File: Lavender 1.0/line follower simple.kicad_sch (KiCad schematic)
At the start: 40 parts, among them J1 XT30UPB-M, J2 Conn_01x06_Socket, J5 Conn_01x06_Socket, J6 Conn_02x06_Counter_Clockwise, J7 Conn_02x06_Counter_Clockwise, SW2 SW_Push, SW5 SW_Push_DPDT, SW6 SW_Push_DPDT, U21 BNO055

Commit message: started routing
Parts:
- removed D1, D2: LED, LED_THT:LED_D5.0mm, symbol Device:LED
- removed J2, J5: Conn_01x06_Socket, Connector_JST:JST_SH_BM06B-SRSS-TB_1x06-1MP_P1.00mm_Vertical, symbol Connector:Conn_01x06_Socket
- removed J6, J7: Conn_02x06_Counter_Clockwise, Connector_IDC:IDC-Header_2x06_P2.54mm_Vertical_SMD, symbol Connector_Generic:Conn_02x06_Counter_Clockwise
- removed JP1, JP10, JP11, JP12, JP13, JP14, JP15, JP16, JP17, JP18, JP19, JP2, JP20, JP3, JP4, JP5, JP6, JP7, JP8, JP9: SolderJumper_2_Open, Jumper:SolderJumper-2_P1.3mm_Open_RoundedPad1.0x1.5mm, symbol Jumper:SolderJumper_2_Open
- removed R1, R2: 47, Resistor_SMD:R_0603_1608Metric_Pad0.98x0.95mm_HandSolder, symbol Device:R
- removed U21: BNO055, customs:BNO055 module, symbol RM_Footprints:BNO055_7Semi_Module
- added H1, H2, H3, H4: MountingHole, customs:2mm hole, symbol Mechanical:MountingHole
- added J14, J15, J2: Conn_01x20, Connector_FFC-FPC:Amphenol_F32Q-1A7x1-11020_1x20-1MP_P0.5mm_Horizontal, symbol Connector_Generic:Conn_01x20
- added J3, J4: Conn_01x02_Pin, Connector_PinHeader_2.54mm:PinHeader_1x02_P2.54mm_Vertical, symbol Connector:Conn_01x02_Pin
- added U1: 74HC4067, customs:74HC4067-Mux, symbol customs:74HC4067
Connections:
- net +3.3V: now also J14.1 (Pin_1), J14.19 (Pin_19), J14.20 (Pin_20), J15.1 (Pin_1), J15.2 (Pin_2), J15.20 (Pin_20), J2.1 (Pin_1), J2.19 (Pin_19), J2.20 (Pin_20), U1.P24 (VCC)
- net AIN1: no longer TB1.6 (AIN1)
- net AIN2: no longer TB1.7 (AIN2)
- net BAT+: no longer SW5.2 (B), SW5.5 (B)
- net BIN1: no longer TB1.4 (BIN1)
- net BIN2: no longer TB1.3 (BIN2)
- net GND: now also J14.11 (Pin_11), J14.13 (Pin_13), J14.15 (Pin_15), J14.17 (Pin_17), J14.18 (Pin_18), J14.2 (Pin_2), J14.3 (Pin_3), J14.5 (Pin_5), J14.6 (Pin_6), J14.7 (Pin_7), J14.8 (Pin_8), J14.9 (Pin_9), J15.10 (Pin_10), J15.12 (Pin_12), J15.14 (Pin_14), J15.16 (Pin_16), J15.18 (Pin_18), J15.4 (Pin_4), J15.6 (Pin_6), J15.8 (Pin_8), J2.11 (Pin_11), J2.13 (Pin_13), J2.15 (Pin_15), J2.17 (Pin_17), J2.3 (Pin_3), J2.5 (Pin_5), J2.7 (Pin_7), J2.9 (Pin_9), U1.P12 (GND), U1.P15 (EN)
- net Motor1+: now also J3.1 (Pin_1); no longer TB1.13 (M1Out+)
- net Motor1-: now also J3.2 (Pin_2); no longer TB1.12 (M1Out-)
- net Motor2+: now also J4.1 (Pin_1); no longer TB1.10 (M2Out+)
- net Motor2-: now also J4.2 (Pin_2); no longer TB1.11 (M2Out-)
- net PWMA: no longer TB1.8 (PWMA)
- net PWMB: no longer TB1.2 (PWMB)
- net Q1: now also U1.P9 (CHAN0)
- net Q2: now also U1.P8 (CHAN1)
- net Q3: now also U1.P7 (CHAN2)
- net Q4: now also U1.P6 (CHAN3)
- net Q5: now also U1.P5 (CHAN4)
- net Q6: now also U1.P4 (CHAN5)
- net Q7: now also U1.P3 (CHAN6)
- net Q8: now also U1.P2 (CHAN7)
- net Q9: now also U1.P23 (CHAN8)
- net SNSR1: now also J15.3 (Pin_3)
- net SNSR2: now also J15.5 (Pin_5)
- net SNSR3: now also J15.7 (Pin_7)
- net SNSR4: now also J15.9 (Pin_9)
- net SNSR5: now also J15.13 (Pin_13)
- net SNSR6: now also J15.15 (Pin_15)
- net SNSR7: now also J15.17 (Pin_17)
- net SNSR8: now also J15.19 (Pin_19)
- net SNSR9: now also J15.11 (Pin_11)
- net T1: now also J2.18 (Pin_18)
- net T2: now also J2.16 (Pin_16)
- net T3: now also J2.14 (Pin_14)
- net T4: now also J2.12 (Pin_12)
- net T5: now also J2.8 (Pin_8)
- net T6: now also J2.6 (Pin_6)
- net T7: now also J2.4 (Pin_4)
- net T8: now also J2.2 (Pin_2)
- net T9: now also J2.10 (Pin_10)
- net IMU_RST: no longer names the net of BlackPill1.4 (PB10)
- net IMU_SCL: no longer names the net of BlackPill1.36 (PB8)
- net IMU_SDA: no longer names the net of BlackPill1.37 (PB9)
- net LED: no longer names the net of BlackPill1.30 (PA15)
- new net AIN1_t: TB1.6 (AIN1)
- new net AIN2_t: TB1.7 (AIN2)
- new net BAT+_t: SW5.2 (B), SW5.5 (B)
- new net BIN1_t: TB1.4 (BIN1)
- new net BIN2_t: TB1.3 (BIN2)
- new net COM_mux: J14.4 (Pin_4), U1.P1 (COM)
- new net Motor1+_t: TB1.13 (M1Out+)
- new net Motor1-_t: TB1.12 (M1Out-)
- new net Motor2+_t: TB1.10 (M2Out+)
- new net Motor2-_t: TB1.11 (M2Out-)
- new net PWMA_t: TB1.8 (PWMA)
- new net PWMB_t: TB1.2 (PWMB)
- new net Q10: U1.P22 (CHAN9)
- new net Q11: U1.P21 (CHAN10)
- new net Q12: U1.P20 (CHAN11)
- new net Q13: U1.P19 (CHAN12)
- new net Q14: U1.P18 (CHAN13)
- new net Q15: U1.P17 (CHAN14)
- new net Q16: U1.P16 (CHAN15)
- new net S0_mux: J14.16 (Pin_16), U1.P10 (S0)
- new net S1_mux: J14.14 (Pin_14), U1.P11 (S1)
- new net S2_mux: J14.12 (Pin_12), U1.P14 (S2)
- new net S3_mux: J14.10 (Pin_10), U1.P13 (S3)
- no-connect marks 21 -> 20
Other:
- added sheet Layer connectors (layerconnect.kicad_sch)
- note added: "Mounting holes"
- note added: "Multiplexer"
- note removed: "BNO055 Module"
- note removed: "LEDs"
- note removed: "Sensor Power bus"
- moved on the sheet: BT2, SW5, SW6

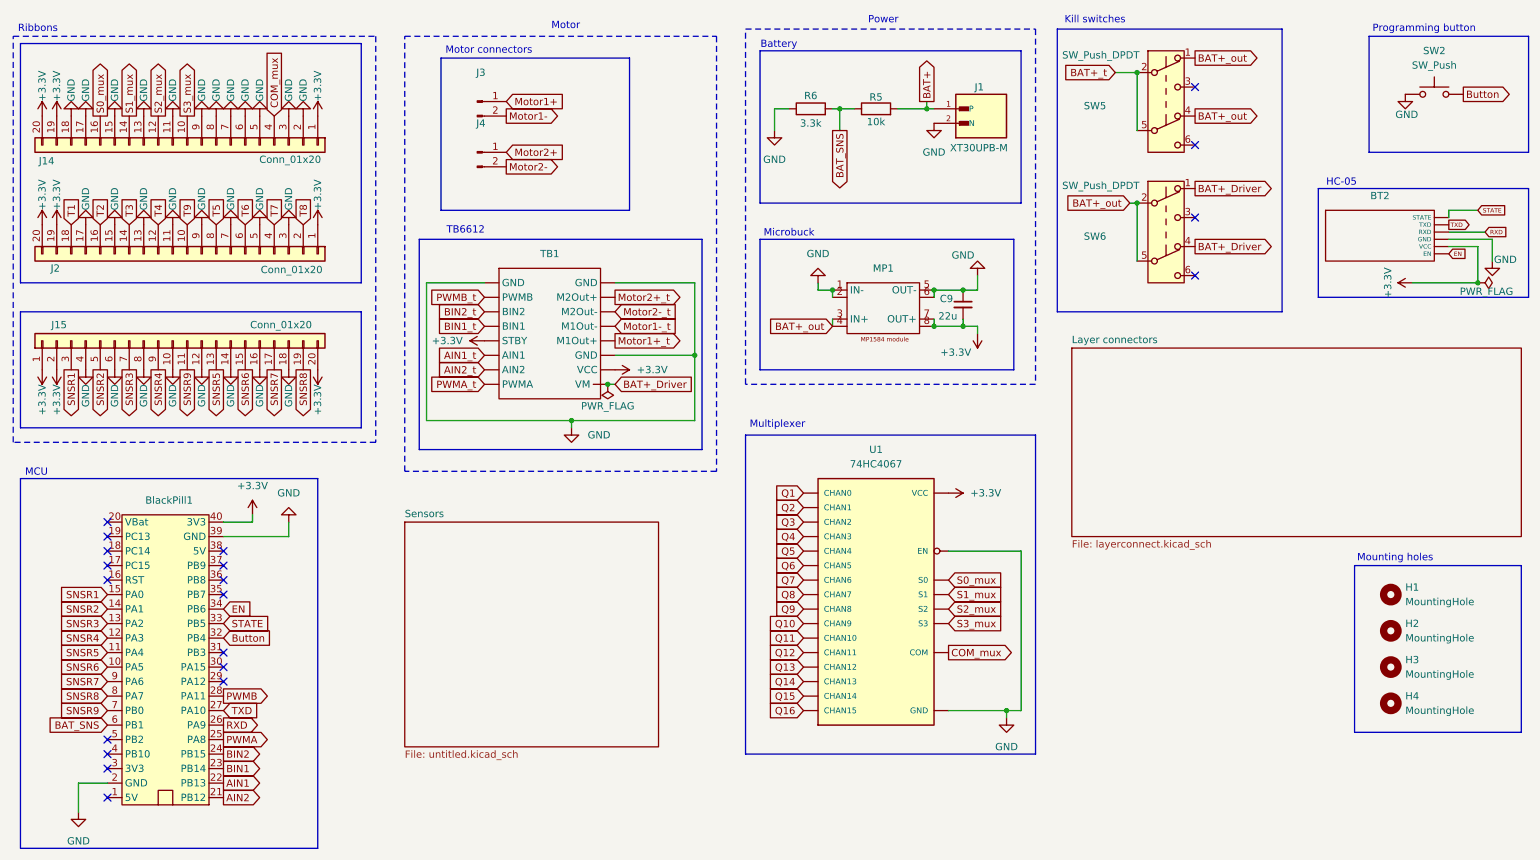
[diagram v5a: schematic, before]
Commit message: Finished 16 sensor array
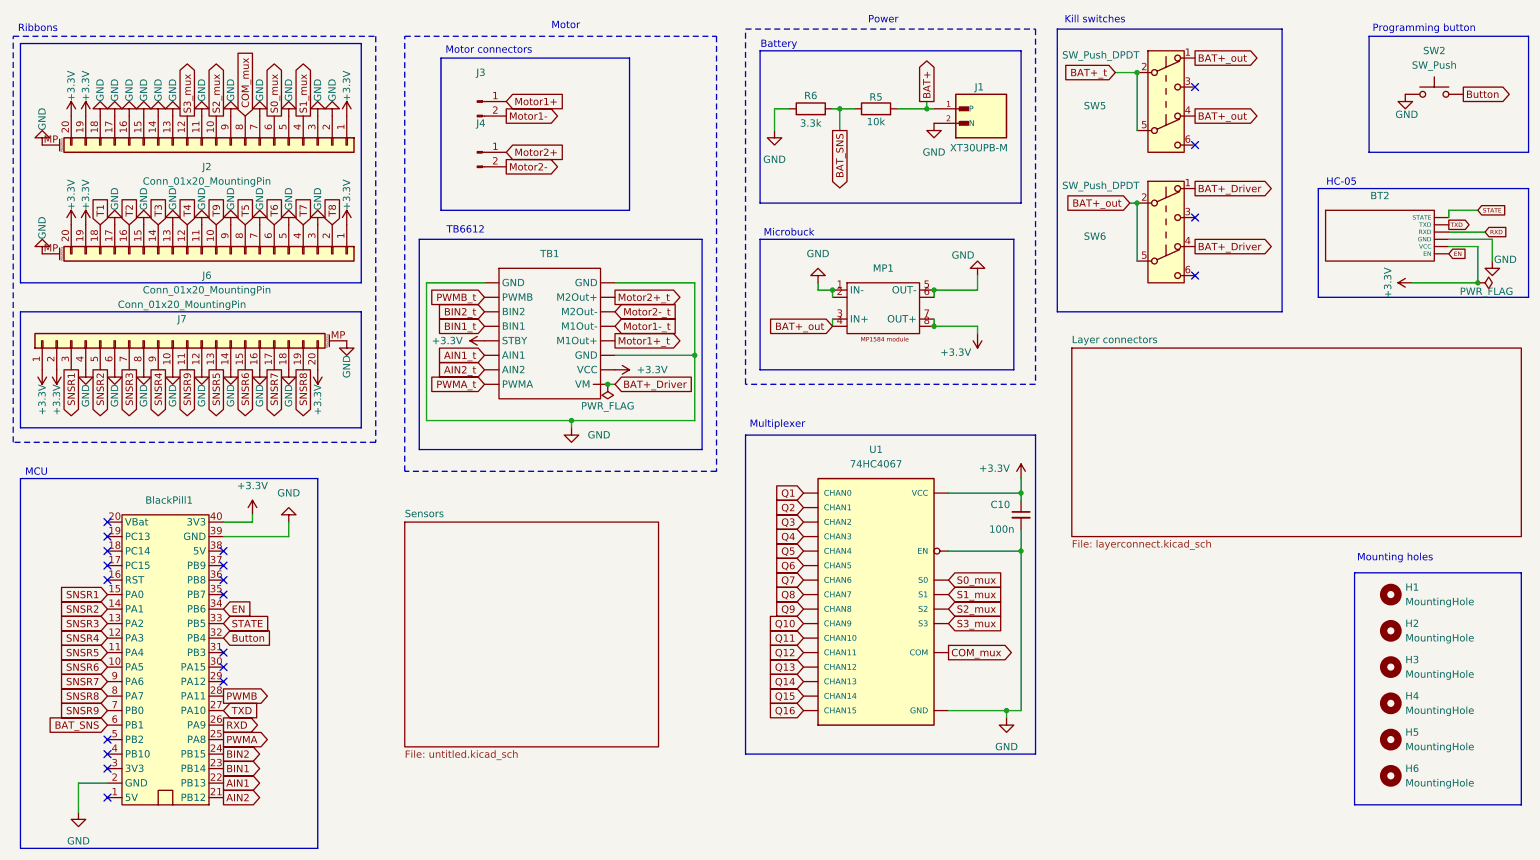
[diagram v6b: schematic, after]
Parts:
- removed C9: 22u, Capacitor_SMD:C_0603_1608Metric_Pad1.08x0.95mm_HandSolder, symbol Device:C_Small
- removed J14, J15, J2: Conn_01x20, Connector_FFC-FPC:Amphenol_F32Q-1A7x1-11020_1x20-1MP_P0.5mm_Horizontal, symbol Connector_Generic:Conn_01x20
- added C10: 100n, Capacitor_SMD:C_0603_1608Metric_Pad1.08x0.95mm_HandSolder, symbol Device:C_Small
- added H5, H6: MountingHole, customs:2mm hole, symbol Mechanical:MountingHole
- added J2, J6, J7: Conn_01x20_MountingPin, Connector_FFC-FPC:Amphenol_F32Q-1A7x1-11020_1x20-1MP_P0.5mm_Horizontal, symbol Connector_Generic_MountingPin:Conn_01x20_MountingPin
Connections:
- net +3.3V: now also C10.1, J2.1 (Pin_1), J2.19 (Pin_19), J2.20 (Pin_20), J6.1 (Pin_1), J6.19 (Pin_19), J6.20 (Pin_20), J7.1 (Pin_1), J7.2 (Pin_2), J7.20 (Pin_20)
- net COM_mux: now also J2.8 (Pin_8)
- net GND: now also C10.2, J2.11 (Pin_11), J2.13 (Pin_13), J2.14 (Pin_14), J2.15 (Pin_15), J2.16 (Pin_16), J2.17 (Pin_17), J2.18 (Pin_18), J2.2 (Pin_2), J2.3 (Pin_3), J2.5 (Pin_5), J2.7 (Pin_7), J2.9 (Pin_9), J2.MP (MountPin), J6.11 (Pin_11), J6.13 (Pin_13), J6.15 (Pin_15), J6.17 (Pin_17), J6.3 (Pin_3), J6.5 (Pin_5), J6.7 (Pin_7), J6.9 (Pin_9), J6.MP (MountPin), J7.10 (Pin_10), J7.12 (Pin_12), J7.14 (Pin_14), J7.16 (Pin_16), J7.18 (Pin_18), J7.4 (Pin_4), J7.6 (Pin_6), J7.8 (Pin_8), J7.MP (MountPin)
- net S0_mux: now also J2.6 (Pin_6)
- net S1_mux: now also J2.4 (Pin_4)
- net S2_mux: now also J2.10 (Pin_10)
- net S3_mux: now also J2.12 (Pin_12)
- net SNSR1: now also J7.3 (Pin_3)
- net SNSR2: now also J7.5 (Pin_5)
- net SNSR3: now also J7.7 (Pin_7)
- net SNSR4: now also J7.9 (Pin_9)
- net SNSR5: now also J7.13 (Pin_13)
- net SNSR6: now also J7.15 (Pin_15)
- net SNSR7: now also J7.17 (Pin_17)
- net SNSR8: now also J7.19 (Pin_19)
- net SNSR9: now also J7.11 (Pin_11)
- net T1: now also J6.18 (Pin_18)
- net T2: now also J6.16 (Pin_16)
- net T3: now also J6.14 (Pin_14)
- net T4: now also J6.12 (Pin_12)
- net T5: now also J6.8 (Pin_8)
- net T6: now also J6.6 (Pin_6)
- net T7: now also J6.4 (Pin_4)
- net T8: now also J6.2 (Pin_2)
- net T9: now also J6.10 (Pin_10)

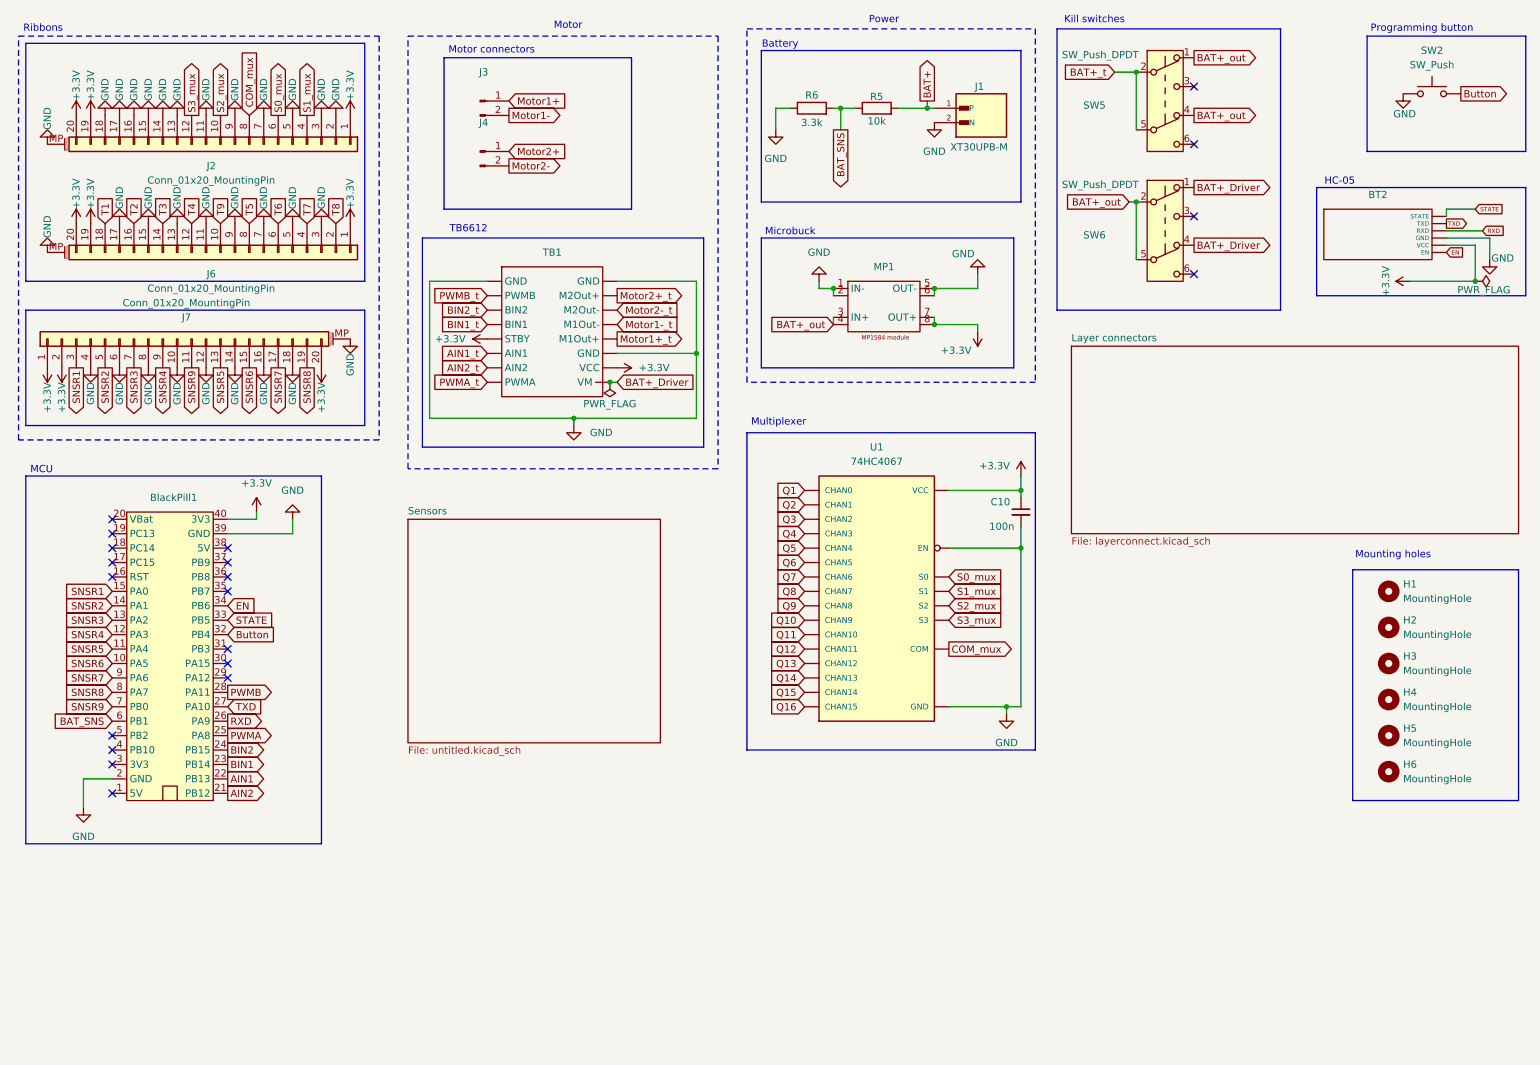
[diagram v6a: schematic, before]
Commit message: Start third sensor array
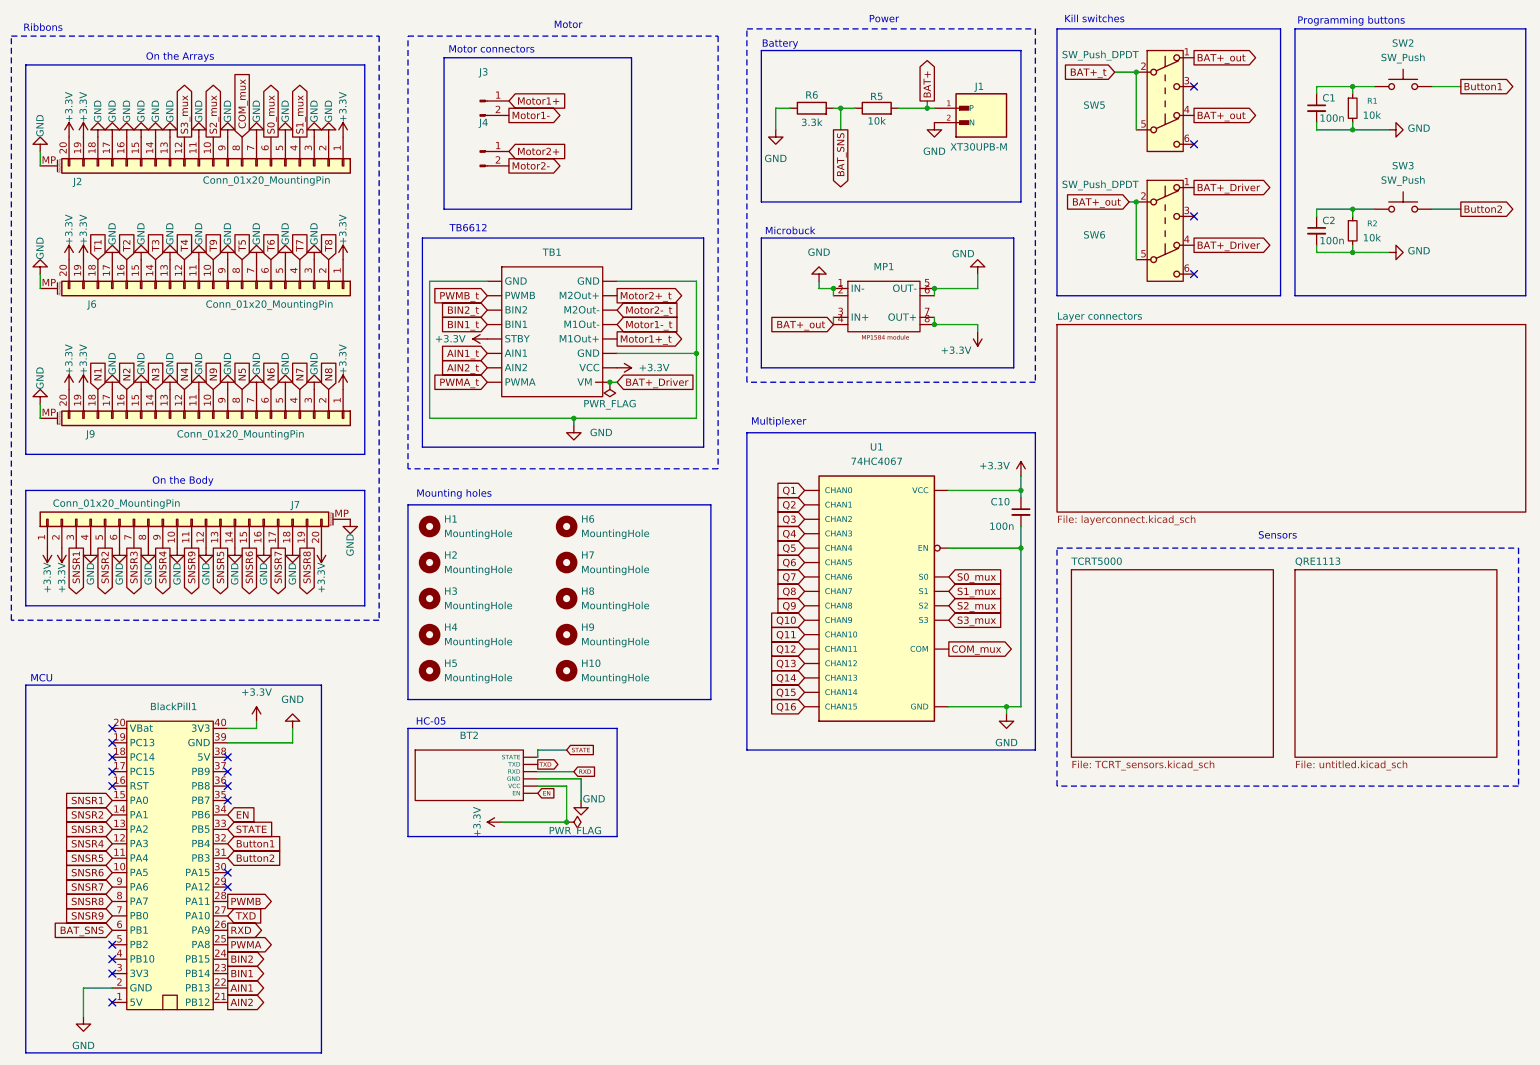
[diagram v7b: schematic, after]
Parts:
- added C1, C2: 100n, Capacitor_SMD:C_0603_1608Metric_Pad1.08x0.95mm_HandSolder, symbol Device:C_Small
- added H10, H7, H8, H9: MountingHole, customs:2mm hole, symbol Mechanical:MountingHole
- added J9: Conn_01x20_MountingPin, Connector_FFC-FPC:Amphenol_F32Q-1A7x1-11020_1x20-1MP_P0.5mm_Horizontal, symbol Connector_Generic_MountingPin:Conn_01x20_MountingPin
- added R1, R2: 10k, Resistor_SMD:R_0603_1608Metric_Pad0.98x0.95mm_HandSolder, symbol Device:R_Small
- added SW3: SW_Push, customs:Push button-fp, symbol Switch:SW_Push
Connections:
- net +3.3V: now also J9.1 (Pin_1), J9.19 (Pin_19), J9.20 (Pin_20)
- net GND: now also C1.2, C2.2, J9.11 (Pin_11), J9.13 (Pin_13), J9.15 (Pin_15), J9.17 (Pin_17), J9.3 (Pin_3), J9.5 (Pin_5), J9.7 (Pin_7), J9.9 (Pin_9), J9.MP (MountPin), R1.2, R2.2; no longer SW2.1
- net Button2: now reaches BlackPill1.31 (PB3)
- net Button2: now also SW3.2
- net Button renamed Button1
- new net: C1.1, R1.1, SW2.1
- new net: C2.1, R2.1, SW3.1
- new net N1: J9.18 (Pin_18)
- new net N2: J9.16 (Pin_16)
- new net N3: J9.14 (Pin_14)
- new net N4: J9.12 (Pin_12)
- new net N5: J9.8 (Pin_8)
- new net N6: J9.6 (Pin_6)
- new net N7: J9.4 (Pin_4)
- new net N8: J9.2 (Pin_2)
- new net N9: J9.10 (Pin_10)
- no-connect marks 20 -> 19
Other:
- sheet Sensors renamed QRE1113
- added sheet TCRT5000 (TCRT_sensors.kicad_sch)
- note added: "On the Arrays"
- note added: "On the Body"
- note added: "Programming buttons"
- note added: "Sensors"
- note removed: "Programming button"
- moved on the sheet: BT2, BlackPill1, H1, H2, H3, H4, H5, H6, J2, J6, J7, SW2
